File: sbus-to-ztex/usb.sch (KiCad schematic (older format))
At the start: 13 parts

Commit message: Commit first go at v1.2
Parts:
- FB1: renamed from FB?; MPN 742792022 -> PZ2012U221-2R0TF; MPN-ALT (none) -> 742792022
- R10, R9: renamed from R?; MPN ERJ-3EKF27R0V -> 0603WAF270JT5E; MPN-ALT (none) -> ERJ-3EKF27R0V
- R15: renamed from R?; value 10k -> 15k; MPN 0603WAF1002T5E -> 0603WAF1502T5E
- gave numbers to parts that had none: 9
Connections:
- net USB_EN: now also R18.1
- net VBus_USB0: now reaches C3.1, FB1.2, J4.1 (VBUS)
- net +3.3V renamed +3V3
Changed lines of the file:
@@
 $EndDescr
 $Comp
-L Connector:USB_B_Micro J?
+L Connector:USB_B_Micro J4
 U 1 1 60D9A6A3
 P 5000 2800
-F 0 "J?" H 5055 3267 50  0000 C CNN
+F 0 "J4" H 5055 3267 50  0000 C CNN
 F 1 "USB_B_Micro" H 5055 3176 50  0000 C CNN
 F 2 "Connector_USB:USB_Micro-B_Molex-105017-0001" H 5150 2750 50  0001 C CNN
@@
 $EndComp
 $Comp
-L Power_Management:TPS2041B U?
+L Power_Management:TPS2041B U7
 U 1 1 60D9A6AC
 P 6700 2800
-F 0 "U?" H 6700 3267 50  0000 C CNN
+F 0 "U7" H 6700 3267 50  0000 C CNN
 F 1 "TPS2065" H 6700 3176 50  0000 C CNN
 F 2 "Package_TO_SOT_SMD:SOT-23-5" H 6700 3300 50  0001 C CNN
@@
 	7400 2800 7200 2800
 $Comp
-L power:GND #PWR?
+L power:GND #PWR0126
 U 1 1 60D9A6B5
 P 6700 3400
-F 0 "#PWR?" H 6700 3150 50  0001 C CNN
+F 0 "#PWR0126" H 6700 3150 50  0001 C CNN
 F 1 "GND" H 6705 3227 50  0000 C CNN
 F 2 "" H 6700 3400 50  0001 C CNN
@@
 Wire Wire Line
 	6200 2600 6000 2600
-Wire Wire Line
-	6200 3000 6000 3000
 Text Label 6000 2600 2    50   ~ 0
 USB_FLT
@@
 AR Path="/5F679B53/60D9A6C2" Ref="R?"  Part="1"
 AR Path="/5F69F4EF/60D9A6C2" Ref="R?"  Part="1"
-F 0 "R?" V 6280 2450 50  0000 C CNN
+AR Path="/60D72F2C/60D9A6C2" Ref="R19"  Part="1"
+F 0 "R19" V 6280 2450 50  0000 C CNN
 F 1 "10k" V 6200 2450 50  0000 C CNN
 F 2 "Resistor_SMD:R_0603_1608Metric" V 6130 2450 50  0001 C CNN
@@
 	6200 2300 6200 2100
 Text GLabel 6250 2100 2    50   Input ~ 0
-+3.3V
++3V3
 $Comp
 L Device:R R?
@@
 AR Path="/5F679B53/60D9A6CD" Ref="R?"  Part="1"
 AR Path="/5F69F4EF/60D9A6CD" Ref="R?"  Part="1"
-F 0 "R?" V 6180 2850 50  0000 C CNN
+AR Path="/60D72F2C/60D9A6CD" Ref="R18"  Part="1"
+F 0 "R18" V 6180 2850 50  0000 C CNN
 F 1 "10k" V 6100 2850 50  0000 C CNN
 F 2 "Resistor_SMD:R_0603_1608Metric" V 6030 2850 50  0001 C CNN
@@
 AR Path="/5F679B53/60D9A6E1" Ref="C?"  Part="1"
 AR Path="/5F69F4EF/60D9A6E1" Ref="C?"  Part="1"
-F 0 "C?" H 7225 2100 50  0000 L CNN
+AR Path="/60D72F2C/60D9A6E1" Ref="C5"  Part="1"
+F 0 "C5" H 7225 2100 50  0000 L CNN
 F 1 "100nF" H 7225 1900 50  0000 L CNN
 F 2 "Capacitor_SMD:C_0603_1608Metric" H 7238 1850 50  0001 C CNN
@@
 $EndComp
 $Comp
-L power:GND #PWR?
+L power:GND #PWR0127
 U 1 1 60D9A6E8
 P 7200 2150
-F 0 "#PWR?" H 7200 1900 50  0001 C CNN
+F 0 "#PWR0127" H 7200 1900 50  0001 C CNN
 F 1 "GND" H 7205 1977 50  0000 C CNN
 F 2 "" H 7200 2150 50  0001 C CNN
@@
 AR Path="/5F679B53/60D9A6EF" Ref="R?"  Part="1"
 AR Path="/5F69F4EF/60D9A6EF" Ref="R?"  Part="1"
-F 0 "R?" V 7280 2950 50  0000 C CNN
+AR Path="/60D72F2C/60D9A6EF" Ref="R20"  Part="1"
+F 0 "R20" V 7280 2950 50  0000 C CNN
 F 1 "1k" V 7200 2950 50  0000 C CNN
 F 2 "Resistor_SMD:R_0603_1608Metric" V 7130 2950 50  0001 C CNN
@@
 	4700 2800 4450 2800
 $Comp
-L Power_Protection:SN65220 U?
+L Power_Protection:SN65220 U5
 U 1 1 60D9A6FD
 P 4250 2850
-F 0 "U?" V 4296 2937 50  0000 L CNN
+F 0 "U5" V 4296 2937 50  0000 L CNN
 F 1 "SN65220" V 4205 2937 50  0000 L CNN
 F 2 "Package_TO_SOT_SMD:SOT-23-6" H 4600 2700 50  0001 L CNN
@@
 	4450 2900 4450 3450
 $Comp
-L power:GND #PWR?
+L power:GND #PWR0128
 U 1 1 60D9A706
 P 3850 2850
-F 0 "#PWR?" H 3850 2600 50  0001 C CNN
+F 0 "#PWR0128" H 3850 2600 50  0001 C CNN
 F 1 "GND" H 3855 2677 50  0000 C CNN
 F 2 "" H 3850 2850 50  0001 C CNN
@@
 AR Path="/5F679B53/60D9A70F" Ref="R?"  Part="1"
 AR Path="/5F69F4EF/60D9A70F" Ref="R?"  Part="1"
-F 0 "R?" V 4030 2500 50  0000 C CNN
+AR Path="/60D72F2C/60D9A70F" Ref="R14"  Part="1"
+F 0 "R14" V 4030 2500 50  0000 C CNN
 F 1 "15k" V 3950 2500 50  0000 C CNN
 F 2 "Resistor_SMD:R_0603_1608Metric" V 3880 2500 50  0001 C CNN
@@
 AR Path="/5F679B53/60D9A717" Ref="R?"  Part="1"
 AR Path="/5F69F4EF/60D9A717" Ref="R?"  Part="1"
-F 0 "R?" V 4030 3200 50  0000 C CNN
-F 1 "10k" V 3950 3200 50  0000 C CNN
+AR Path="/60D72F2C/60D9A717" Ref="R15"  Part="1"
+F 0 "R15" V 4030 3200 50  0000 C CNN
+F 1 "15k" V 3950 3200 50  0000 C CNN
 F 2 "Resistor_SMD:R_0603_1608Metric" V 3880 3200 50  0001 C CNN
 F 3 "" H 3950 3200 50  0000 C CNN
-F 4 "0603WAF1002T5E" V 3950 2600 50  0001 C CNN "MPN"
+F 4 "0603WAF1502T5E" V 3950 2600 50  0001 C CNN "MPN"
 	1    3950 3200
 	-1   0    0    1
@@
 AR Path="/5F679B53/60D9A72D" Ref="R?"  Part="1"
 AR Path="/5F69F4EF/60D9A72D" Ref="R?"  Part="1"
-F 0 "R?" V 3780 2250 50  0000 C CNN
+AR Path="/60D72F2C/60D9A72D" Ref="R9"  Part="1"
+F 0 "R9" V 3780 2250 50  0000 C CNN
 F 1 "27" V 3700 2250 50  0000 C CNN
 F 2 "Resistor_SMD:R_0603_1608Metric" V 3630 2250 50  0001 C CNN
 F 3 "" H 3700 2250 50  0000 C CNN
-F 4 "ERJ-3EKF27R0V" V 3700 1650 50  0001 C CNN "MPN"
+F 4 "0603WAF270JT5E" V 3700 2250 50  0001 C CNN "MPN"
+F 5 "ERJ-3EKF27R0V" V 3700 1650 50  0001 C CNN "MPN-ALT"
 	1    3700 2250
 	0    1    1    0
@@
 AR Path="/5F679B53/60D9A735" Ref="R?"  Part="1"
 AR Path="/5F69F4EF/60D9A735" Ref="R?"  Part="1"
-F 0 "R?" V 3780 3450 50  0000 C CNN
+AR Path="/60D72F2C/60D9A735" Ref="R10"  Part="1"
+F 0 "R10" V 3780 3450 50  0000 C CNN
 F 1 "27" V 3700 3450 50  0000 C CNN
 F 2 "Resistor_SMD:R_0603_1608Metric" V 3630 3450 50  0001 C CNN
 F 3 "" H 3700 3450 50  0000 C CNN
-F 4 "ERJ-3EKF27R0V" V 3700 2850 50  0001 C CNN "MPN"
+F 4 "0603WAF270JT5E" V 3700 3450 50  0001 C CNN "MPN"
+F 5 "ERJ-3EKF27R0V" V 3700 2850 50  0001 C CNN "MPN-ALT"
 	1    3700 3450
 	0    1    1    0
@@
 	3850 2250 3950 2250
 Connection ~ 3950 2250
-Text Label 3550 2250 2    50   ~ 0
-USBH0_D+
-Text Label 3550 3450 2    50   ~ 0
-USBH0_D-
 Text Label 4950 1450 2    50   ~ 0
 VBus
@@
 Connection ~ 5000 3200
 $Comp
-L power:GND #PWR?
+L power:GND #PWR0129
 U 1 1 60D9A747
 P 5000 3200
-F 0 "#PWR?" H 5000 2950 50  0001 C CNN
+F 0 "#PWR0129" H 5000 2950 50  0001 C CNN
 F 1 "GND" H 5005 3027 50  0000 C CNN
 F 2 "" H 5000 3200 50  0001 C CNN
@@
 	4700 1850 4950 1850
 $Comp
-L Device:CP C?
+L Device:CP C3
 U 1 1 60D9A750
 P 4950 2000
-F 0 "C?" H 5068 2046 50  0000 L CNN
+F 0 "C3" H 5068 2046 50  0000 L CNN
 F 1 "CP" H 5068 1955 50  0000 L CNN
 F 2 "Capacitor_SMD:C_1206_3216Metric" H 4988 1850 50  0001 C CNN
@@
 $EndComp
 $Comp
-L Device:Ferrite_Bead_Small FB?
+L Device:Ferrite_Bead_Small FB1
 U 1 1 60D9A758
 P 4950 1750
-F 0 "FB?" H 5050 1796 50  0000 L CNN
+F 0 "FB1" H 5050 1796 50  0000 L CNN
 F 1 "Ferrite_Bead_Small" H 5050 1705 50  0000 L CNN
 F 2 "Inductor_SMD:L_0805_2012Metric" V 4880 1750 50  0001 C CNN
 F 3 "~" H 4950 1750 50  0001 C CNN
-F 4 "742792022" H 4950 1750 50  0001 C CNN "MPN"
+F 4 "742792022" H 4950 1750 50  0001 C CNN "MPN-ALT"
+F 5 "PZ2012U221-2R0TF" H 4950 1750 50  0001 C CNN "MPN"
 	1    4950 1750
 	1    0    0    -1
@@
 	4950 1650 4950 1450
 $Comp
-L power:GND #PWR?
+L power:GND #PWR0130
 U 1 1 60D9A761
 P 4950 2150
-F 0 "#PWR?" H 4950 1900 50  0001 C CNN
+F 0 "#PWR0130" H 4950 1900 50  0001 C CNN
 F 1 "GND" H 4955 1977 50  0000 C CNN
 F 2 "" H 4950 2150 50  0001 C CNN
@@
 	1    0    0    -1
 $EndComp
+Wire Wire Line
+	6000 3000 6100 3000
+Connection ~ 6100 3000
+Wire Wire Line
+	6100 3000 6200 3000
+Text GLabel 3550 2250 0    50   Input ~ 0
+USBH0_D+
+Text GLabel 3550 3450 0    50   Input ~ 0
+USBH0_D-
+Text Label 4700 2050 2    50   ~ 0
+VBus_USB0
 $EndSCHEMATC

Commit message: fix footprints for SeeedStudio DRC results
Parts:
- J4: DK_Datasheet_Link https://www.molex.com/pdm_docs/sd/1050170001_sd.pdf -> (none)
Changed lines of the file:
@@
 F 4 "WM1399CT-ND" H 5000 2800 50  0001 C CNN "Digi-Key_PN"
 F 5 "1050170001" H 5000 2800 50  0001 C CNN "MPN"
-F 6 "https://www.molex.com/pdm_docs/sd/1050170001_sd.pdf" H 5000 2800 50  0001 C CNN "DK_Datasheet_Link"
-F 7 "CONN RCPT USB2.0 MICRO B SMD R/A" H 5000 2800 50  0001 C CNN "Description"
-F 8 "Molex" H 5000 2800 50  0001 C CNN "Manufacturer"
+F 6 "CONN RCPT USB2.0 MICRO B SMD R/A" H 5000 2800 50  0001 C CNN "Description"
+F 7 "Molex" H 5000 2800 50  0001 C CNN "Manufacturer"
 	1    5000 2800
 	-1   0    0    -1

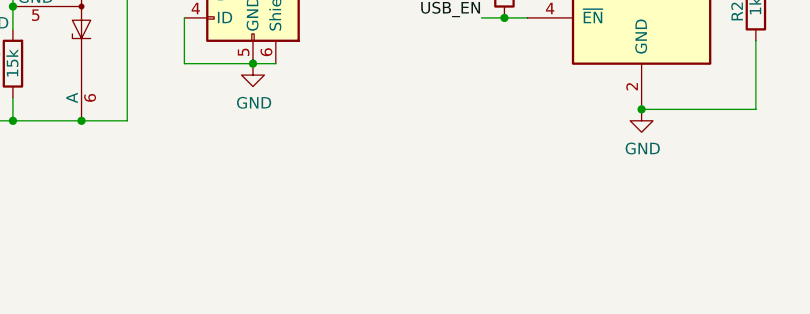
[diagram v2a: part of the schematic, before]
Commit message: fix footprints for SeeedStudio DRC results
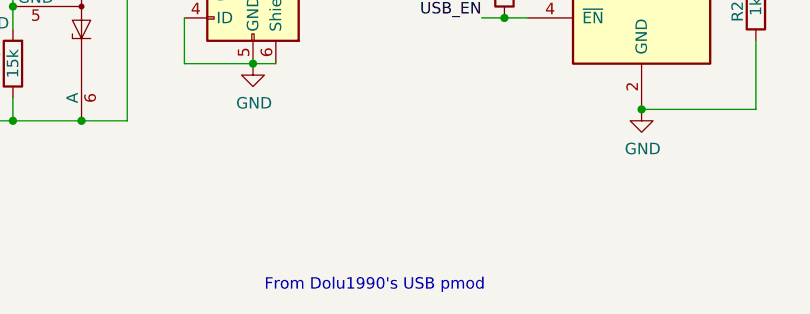
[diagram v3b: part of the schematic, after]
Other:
- note added: "From Dolu1990's USB pmod"
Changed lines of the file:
@@
 Text Label 4700 2050 2    50   ~ 0
 VBus_USB0
+Text Notes 5050 4200 0    50   ~ 0
+From Dolu1990's USB pmod
 $EndSCHEMATC

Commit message: update some MPN w/ SeeedStudio replacement
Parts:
- J4: URL (none) -> https://eu.mouser.com/ProductDetail/Molex/105017-0001?qs=hl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
- U7: URL (none) -> https://eu.mouser.com/ProductDetail/Texas-Instruments/TPS20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
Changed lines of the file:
@@
 F 6 "CONN RCPT USB2.0 MICRO B SMD R/A" H 5000 2800 50  0001 C CNN "Description"
 F 7 "Molex" H 5000 2800 50  0001 C CNN "Manufacturer"
+F 8 "https://eu.mouser.com/ProductDetail/Molex/105017-0001?qs=hlXxxvYE36k7QcsR97GUKA%3D%3D" H 5000 2800 50  0001 C CNN "URL"
 	1    5000 2800
 	-1   0    0    -1
@@
 F 4 "TPS2065CDBVT-2" H 6700 2800 50  0001 C CNN "MPN"
 F 5 "595-TPS2065CDBVT-2" H 6700 2800 50  0001 C CNN "Mouser No"
+F 6 "https://eu.mouser.com/ProductDetail/Texas-Instruments/TPS2065CDBVT-2?qs=jUogulkOmla%2FprItLs6IKw%3D%3D" H 6700 2800 50  0001 C CNN "URL"
 	1    6700 2800
 	1    0    0    -1

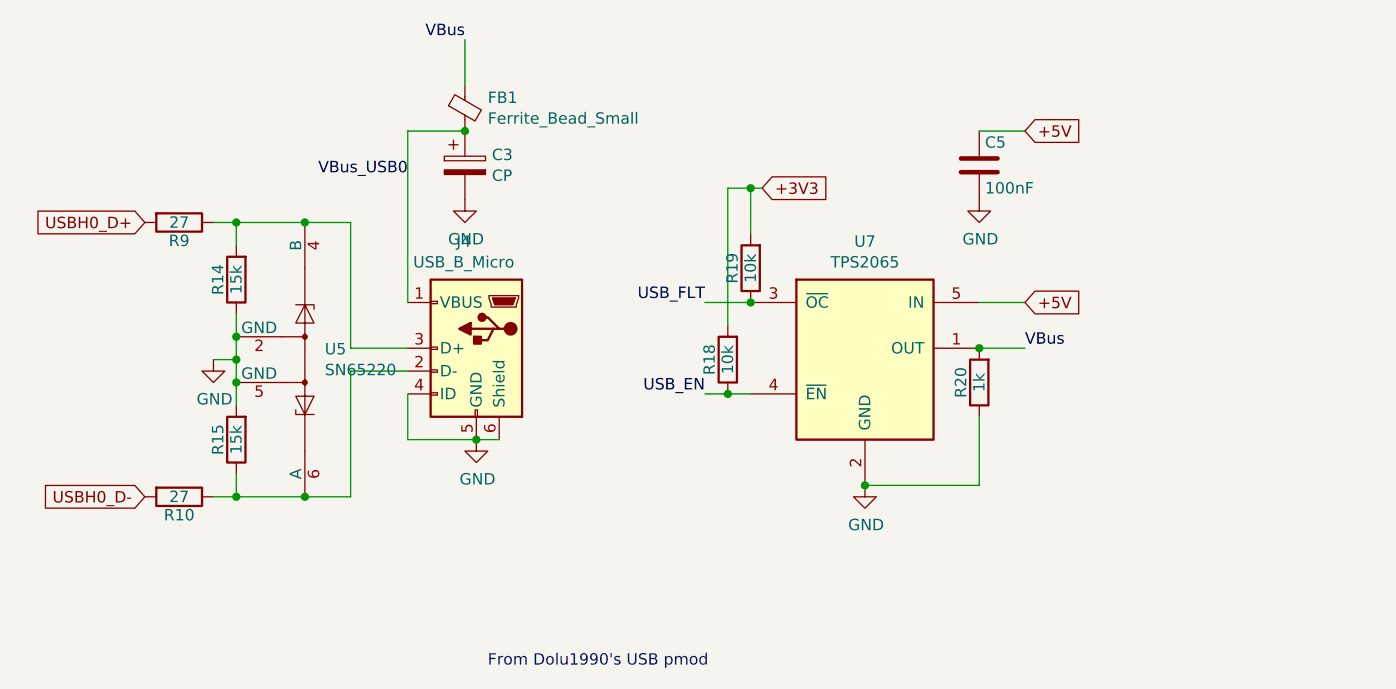
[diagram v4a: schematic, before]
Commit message: Fewer LEDs, more interrupts, replace USB VBus power chip by something that might be available..., update signals file
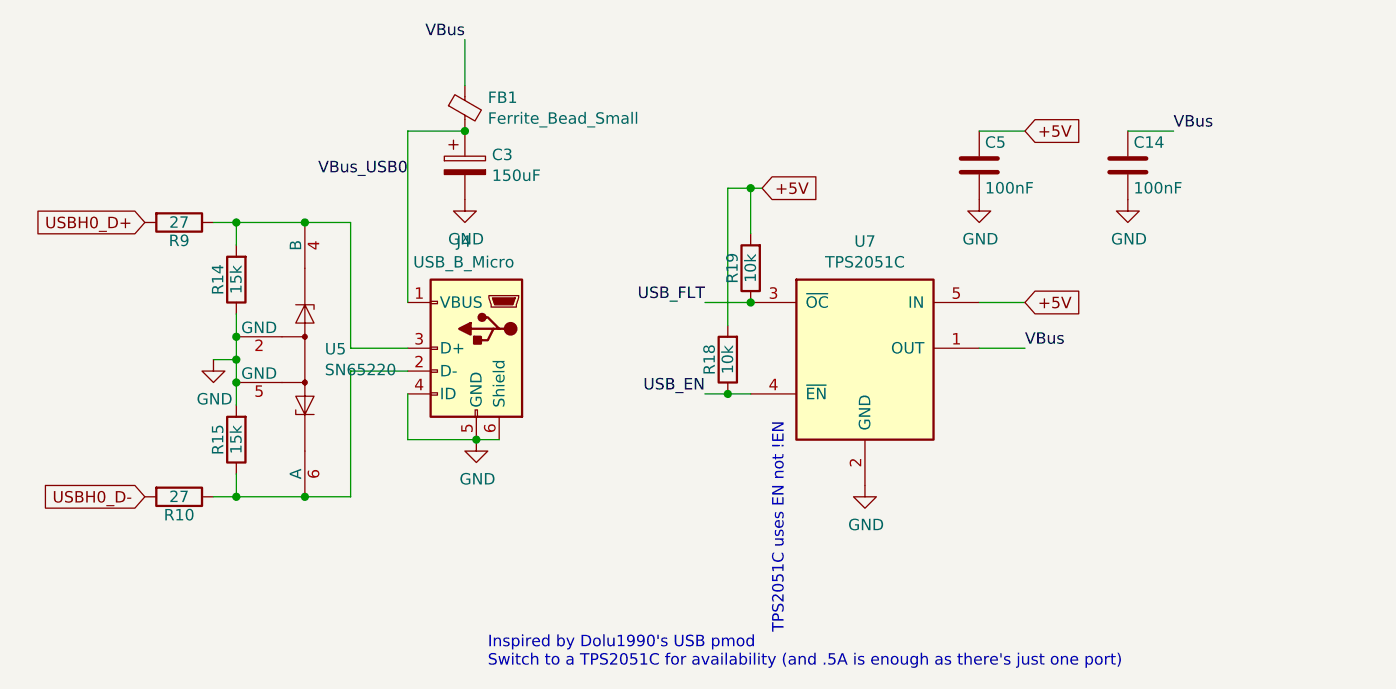
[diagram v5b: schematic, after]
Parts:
- removed R20: 1k, Resistor_SMD:R_0603_1608Metric, symbol Device:R
- added C14: 100nF, Capacitor_SMD:C_0603_1608Metric, symbol Device:C
- C3: value CP -> 150uF
- U7: value TPS2065 -> TPS2051C; MPN TPS2065CDBVT-2 -> TPS2051CDBVR; Mouser No 595-TPS2065CDBVT-2 -> 595-TPS2051CDBVR; URL https://eu.mouser.com/ProductDetail/Texas-Instruments/TPS20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 -> https://www.mouser.fr/ProductDetail/Texas-Instruments/TPS20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
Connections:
- net +3V3 is gone; now on net +5V: R18.2, R19.2
- net GND: now also C14.2
- net VBus: now also C14.1
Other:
- note added: "Inspired by Dolu1990's USB pmod\nSwitch to a TPS2051C for availability (and .5A is enough as there's just one port)\n"
- note added: "TPS2051C uses EN not !EN"
- note removed: "From Dolu1990's USB pmod"
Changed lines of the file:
@@
 	-1   0    0    -1
-$EndComp
-$Comp
-L Power_Management:TPS2041B U7
-U 1 1 60D9A6AC
-P 6700 2800
-F 0 "U7" H 6700 3267 50  0000 C CNN
-F 1 "TPS2065" H 6700 3176 50  0000 C CNN
-F 2 "Package_TO_SOT_SMD:SOT-23-5" H 6700 3300 50  0001 C CNN
-F 3 "" H 6650 3100 50  0001 C CNN
-F 4 "TPS2065CDBVT-2" H 6700 2800 50  0001 C CNN "MPN"
-F 5 "595-TPS2065CDBVT-2" H 6700 2800 50  0001 C CNN "Mouser No"
-F 6 "https://eu.mouser.com/ProductDetail/Texas-Instruments/TPS2065CDBVT-2?qs=jUogulkOmla%2FprItLs6IKw%3D%3D" H 6700 2800 50  0001 C CNN "URL"
-	1    6700 2800
-	1    0    0    -1
 $EndComp
 Text Label 7400 2800 0    50   ~ 0
@@
 	-1   0    0    1
 $EndComp
-Connection ~ 6200 2600
 Wire Wire Line
 	6200 2300 6200 2100
-Text GLabel 6250 2100 2    50   Input ~ 0
-+3V3
 $Comp
 L Device:R R?
@@
 	1    0    0    -1
 $EndComp
-$Comp
-L Device:R R?
-U 1 1 60D9A6EF
-P 7200 2950
-AR Path="/5F6B165A/60D9A6EF" Ref="R?"  Part="1"
-AR Path="/5F679B53/60D9A6EF" Ref="R?"  Part="1"
-AR Path="/5F69F4EF/60D9A6EF" Ref="R?"  Part="1"
-AR Path="/60D72F2C/60D9A6EF" Ref="R20"  Part="1"
-F 0 "R20" V 7280 2950 50  0000 C CNN
-F 1 "1k" V 7200 2950 50  0000 C CNN
-F 2 "Resistor_SMD:R_0603_1608Metric" V 7130 2950 50  0001 C CNN
-F 3 "" H 7200 2950 50  0000 C CNN
-F 4 "0603WAF1001T5E" V 7200 2350 50  0001 C CNN "MPN"
-	1    7200 2950
-	-1   0    0    1
-$EndComp
-Connection ~ 7200 2800
-Wire Wire Line
-	7200 3100 7200 3400
-Wire Wire Line
-	7200 3400 6700 3400
-Connection ~ 6700 3400
 Wire Wire Line
 	4700 2900 4450 2900
@@
 P 4950 2000
 F 0 "C3" H 5068 2046 50  0000 L CNN
-F 1 "CP" H 5068 1955 50  0000 L CNN
+F 1 "150uF" H 5068 1955 50  0000 L CNN
 F 2 "Capacitor_SMD:C_1206_3216Metric" H 4988 1850 50  0001 C CNN
 F 3 "~" H 4950 2000 50  0001 C CNN
@@
 VBus_USB0
 Text Notes 5050 4200 0    50   ~ 0
-From Dolu1990's USB pmod
+Inspired by Dolu1990's USB pmod\nSwitch to a TPS2051C for availability (and .5A is enough as there's just one port)\n
+Text GLabel 6250 2100 2    50   Input ~ 0
++5V
+Text Notes 6350 4050 1    50   ~ 0
+TPS2051C uses EN not !EN
+Wire Wire Line
+	7850 1850 8050 1850
+$Comp
+L Device:C C?
+U 1 1 612D3A06
+P 7850 2000
+AR Path="/5F679B53/612D3A06" Ref="C?"  Part="1"
+AR Path="/5F69F4EF/612D3A06" Ref="C?"  Part="1"
+AR Path="/60D72F2C/612D3A06" Ref="C14"  Part="1"
+F 0 "C14" H 7875 2100 50  0000 L CNN
+F 1 "100nF" H 7875 1900 50  0000 L CNN
+F 2 "Capacitor_SMD:C_0603_1608Metric" H 7888 1850 50  0001 C CNN
+F 3 "" H 7850 2000 50  0000 C CNN
+F 4 "www.yageo.com" H 7850 2000 50  0001 C CNN "MNF1_URL"
+F 5 "CC0603KRX7R8BB104" H 7850 2000 50  0001 C CNN "MPN"
+F 6 "603-CC603KRX7R8BB104" H 7850 2000 50  0001 C CNN "Mouser"
+F 7 "?" H 7850 2000 50  0001 C CNN "Digikey"
+F 8 "?" H 7850 2000 50  0001 C CNN "LCSC"
+F 9 "?" H 7850 2000 50  0001 C CNN "Koncar"
+F 10 "TB" H 7850 2000 50  0001 C CNN "Side"
+	1    7850 2000
+	1    0    0    -1
+$EndComp
+$Comp
+L power:GND #PWR0134
+U 1 1 612D3A0D
+P 7850 2150
+F 0 "#PWR0134" H 7850 1900 50  0001 C CNN
+F 1 "GND" H 7855 1977 50  0000 C CNN
+F 2 "" H 7850 2150 50  0001 C CNN
+F 3 "" H 7850 2150 50  0001 C CNN
+	1    7850 2150
+	1    0    0    -1
+$EndComp
+Text Label 8050 1850 0    50   ~ 0
+VBus
+$Comp
+L Power_Management:TPS2041B U7
+U 1 1 60D9A6AC
+P 6700 2800
+F 0 "U7" H 6700 3267 50  0000 C CNN
+F 1 "TPS2051C" H 6700 3176 50  0000 C CNN
+F 2 "Package_TO_SOT_SMD:SOT-23-5" H 6700 3300 50  0001 C CNN
+F 3 "" H 6650 3100 50  0001 C CNN
+F 4 "TPS2051CDBVR" H 6700 2800 50  0001 C CNN "MPN"
+F 5 "595-TPS2051CDBVR" H 6700 2800 50  0001 C CNN "Mouser No"
+F 6 "https://www.mouser.fr/ProductDetail/Texas-Instruments/TPS2051CDBVR?qs=PF3AD18CSE5vi2HeWLJCmw%3D%3D" H 6700 2800 50  0001 C CNN "URL"
+	1    6700 2800
+	1    0    0    -1
+$EndComp
+Connection ~ 6200 2600
 $EndSCHEMATC

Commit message: USB ID pin left floating
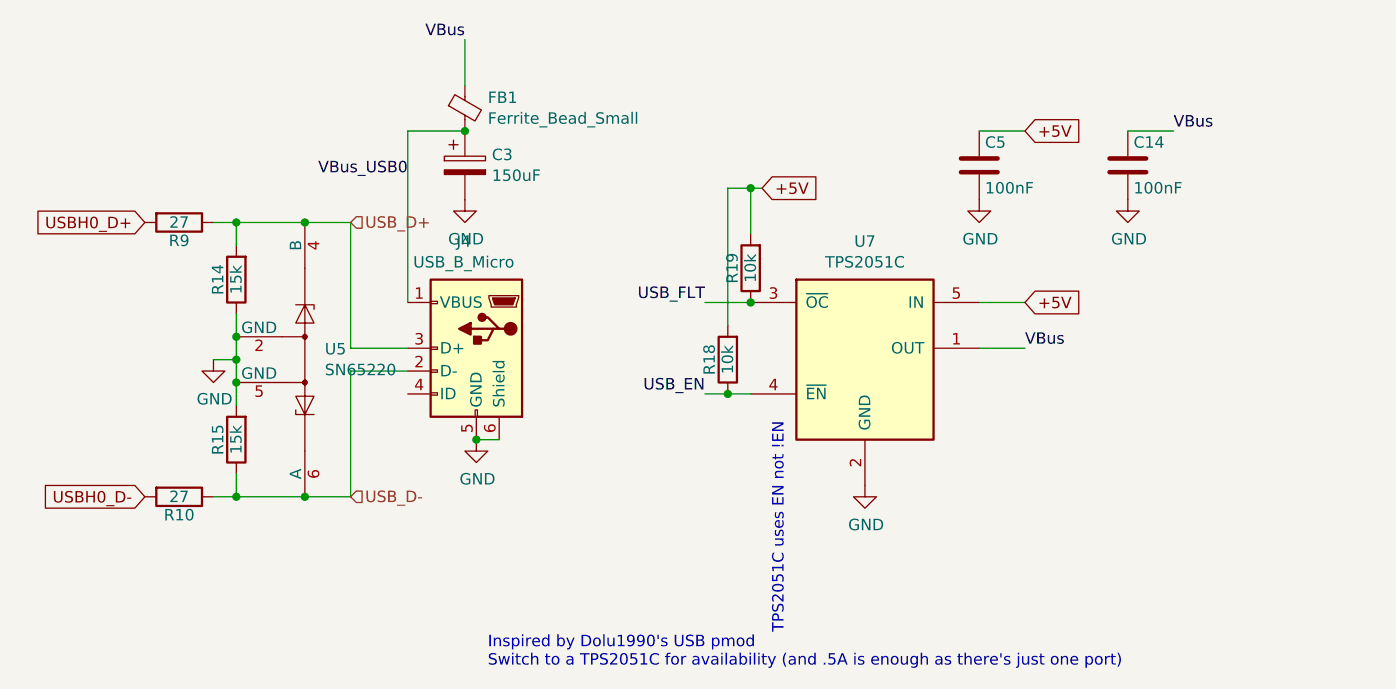
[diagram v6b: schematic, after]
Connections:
- net GND: no longer J4.4 (ID)
- net USB_D-: now reaches J4.2 (D-), R10.1, R15.1, U5.6 (A)
- net USB_D+: now reaches J4.3 (D+), R14.2, R9.1, U5.4 (B)
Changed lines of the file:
@@
 VBus
-Wire Wire Line
-	4700 3000 4700 3200
-Wire Wire Line
-	4700 3200 5000 3200
 Wire Wire Line
 	5000 3200 5100 3200
@@
 $EndComp
 Connection ~ 6200 2600
+Text HLabel 4450 2250 2    50   Input ~ 0
+USB_D+
+Text HLabel 4450 3450 2    50   Input ~ 0
+USB_D-
 $EndSCHEMATC
